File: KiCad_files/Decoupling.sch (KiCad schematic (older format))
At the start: 0 parts

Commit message: Added Decoupling Caps?
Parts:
- added C? (x38): 4.7uF, symbol C_Small
- added C? (x4): 0.1uF, symbol C_Small
- added C? (x51): 0.47uF, symbol C_Small
- added C? (x4): 100uF, symbol C_Small
- added C?: 680uF, symbol CP1_Small
- added C? (x3): 47uF, symbol C_Small
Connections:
- net labels added: GND, MGTAVCC, MGTAVTT, VCCAUX, VCCBRAM, VCCINT
- wire segments 0 -> 255

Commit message: Cleanup + Update to KiCad 5.0 + DDR2
Updated to KiCad 5, which re-organized libraries, so corrected them to not need RASAC-rescue.lib.
Also cleaned up some stuff.
DDR4 has been removed and in place will be DDR2.
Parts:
- C? (x100): symbol C_Small -> Device:C_Small
- C?: symbol CP1_Small -> Device:CP1_Small

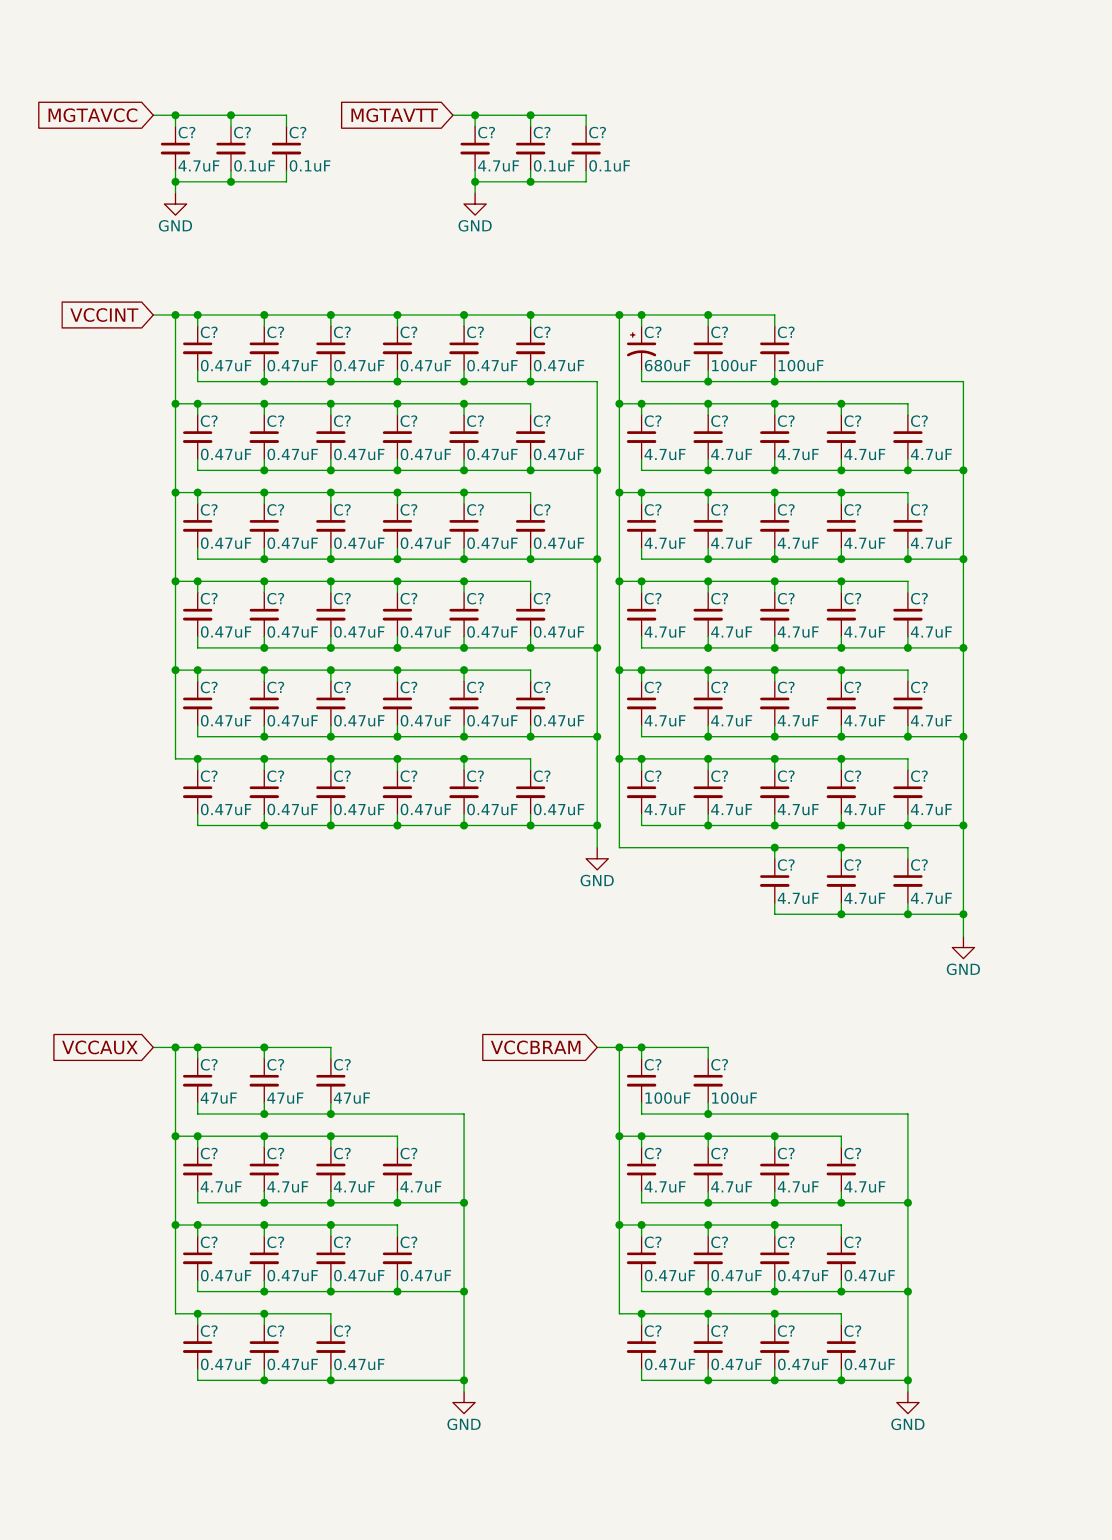
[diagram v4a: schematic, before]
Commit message: Finished HDMI. Added I2C
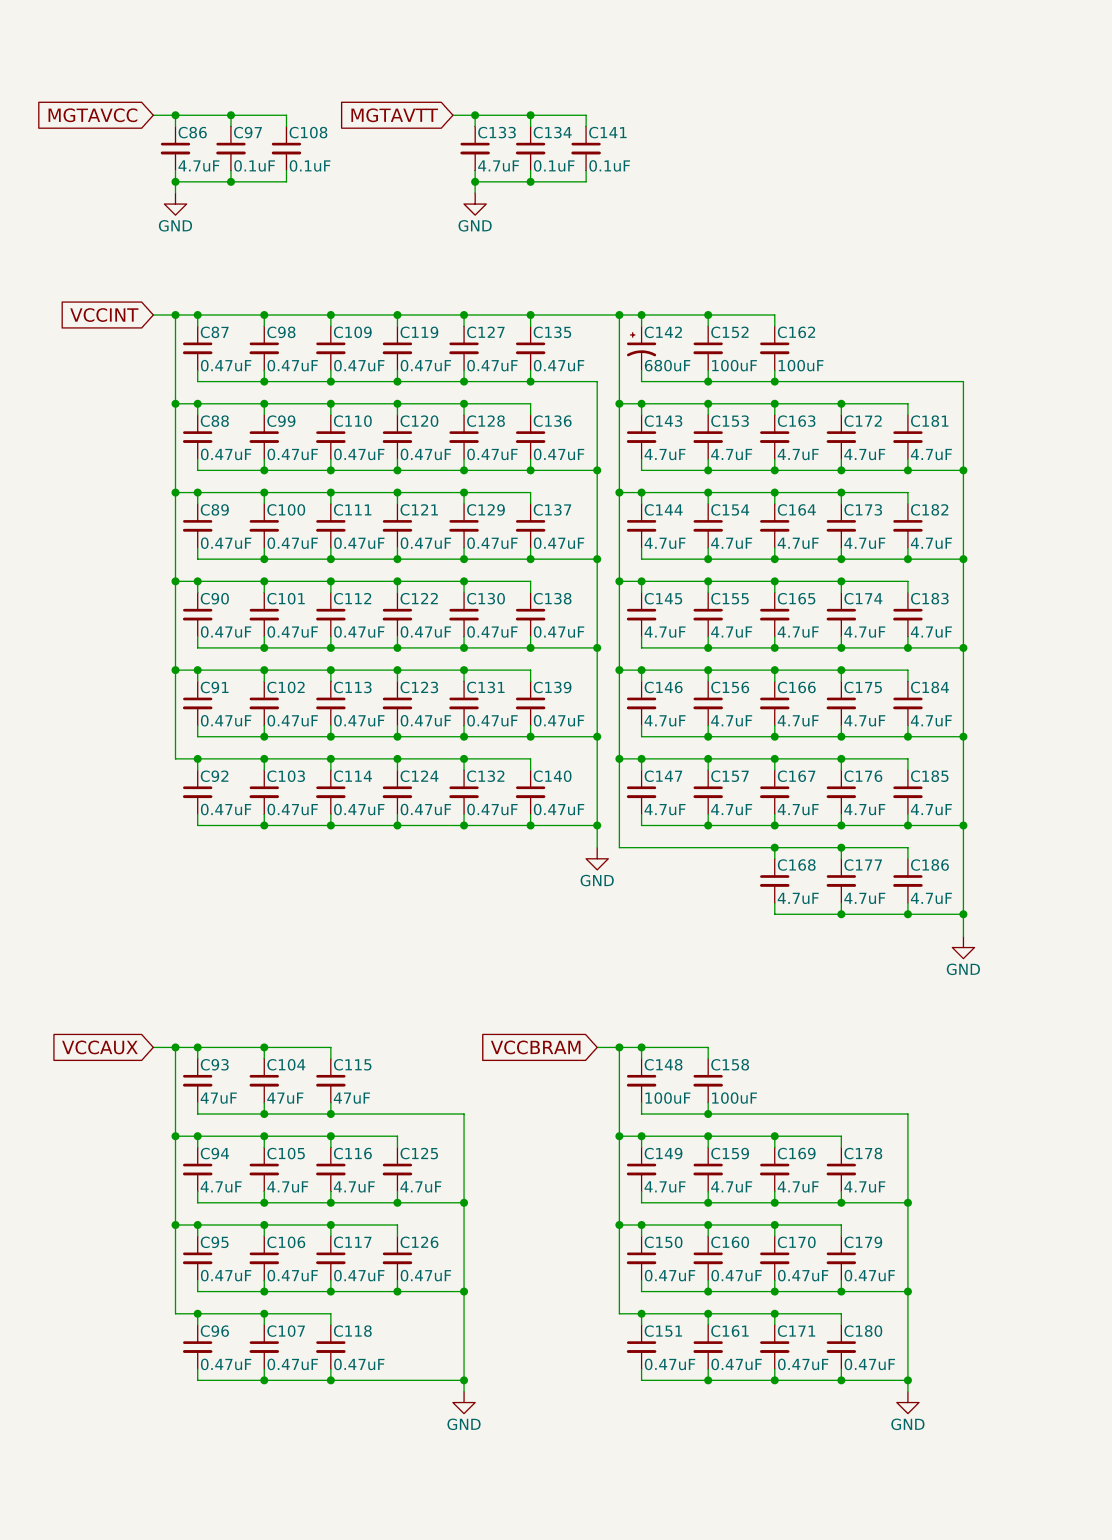
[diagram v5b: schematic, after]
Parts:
- gave numbers to parts that had none: 101
